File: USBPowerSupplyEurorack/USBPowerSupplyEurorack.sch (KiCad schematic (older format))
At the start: 21 parts, among them J1 1734366-1, J2 95278-501A10LF, Q1 Q_PMOS_GSD

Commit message: added LEDs, all components are placed now
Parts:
- D2, D5: footprint (none) -> digikey-footprints:LED_0603
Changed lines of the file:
@@
 F 0 "D2" V 3121 5260 50  0000 R CNN
 F 1 "Blue" V 3030 5260 50  0000 R CNN
-F 2 "" V 3075 5330 50  0001 C CNN
+F 2 "digikey-footprints:LED_0603" V 3075 5330 50  0001 C CNN
 F 3 "~" V 3075 5330 50  0001 C CNN
 	1    3075 5330
@@
 F 0 "D5" V 3121 5850 50  0000 R CNN
 F 1 "Blue" V 3030 5850 50  0000 R CNN
-F 2 "" V 3075 5920 50  0001 C CNN
+F 2 "digikey-footprints:LED_0603" V 3075 5920 50  0001 C CNN
 F 3 "~" V 3075 5920 50  0001 C CNN
 	1    3075 5920

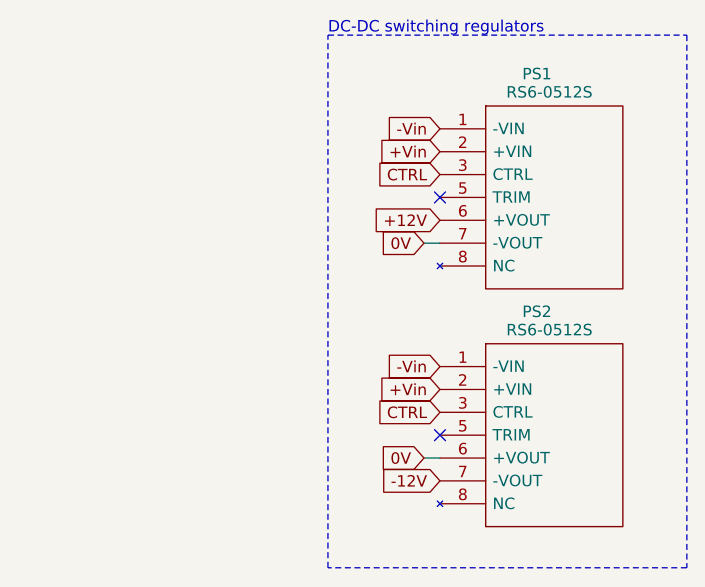
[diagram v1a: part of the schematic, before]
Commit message: new naive routing
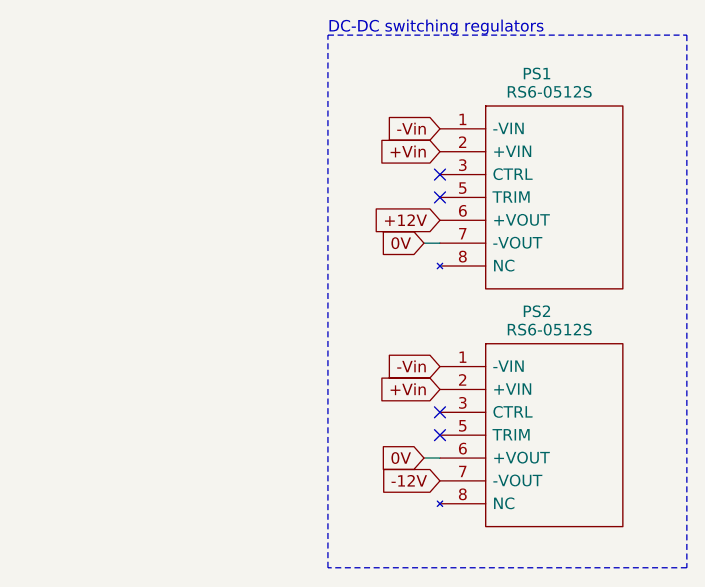
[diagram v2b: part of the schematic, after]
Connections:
- net CTRL: no longer names the net of PS1.3 (CTRL)
- net CTRL: no longer PS2.3 (CTRL)
- no-connect marks 4 -> 6
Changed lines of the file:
@@
 Wire Wire Line
 	8800 3190 8870 3190
-$Comp
-L RS6-0512S:RS6-0512S PS2
-U 1 1 5FE68DDD
-P 8870 3730
-F 0 "PS2" H 9230 3970 50  0000 L CNN
-F 1 "RS6-0512S" H 9160 3890 50  0000 L CNN
-F 2 "RS6-0512S:RS60512S" H 9720 3830 50  0001 L CNN
-F 3 "https://componentsearchengine.com/Datasheets/1/RS6-0512S.pdf" H 9720 3730 50  0001 L CNN
-F 4 "Isolated DC/DC Converters 6W 4.5-9Vin 12Vout 500mA SIP8" H 9720 3630 50  0001 L CNN "Description"
-F 5 "11.6" H 9720 3530 50  0001 L CNN "Height"
-F 6 "RECOM Power" H 9720 3430 50  0001 L CNN "Manufacturer_Name"
-F 7 "RS6-0512S" H 9720 3330 50  0001 L CNN "Manufacturer_Part_Number"
-F 8 "919-RS6-0512S" H 9720 3230 50  0001 L CNN "Mouser Part Number"
-F 9 "https://www.mouser.co.uk/ProductDetail/RECOM-Power/RS6-0512S?qs=FLBwGrBR9%252B1rp7zTwCRMhw%3D%3D" H 9720 3130 50  0001 L CNN "Mouser Price/Stock"
-F 10 "" H 9720 3030 50  0001 L CNN "Arrow Part Number"
-F 11 "" H 9720 2930 50  0001 L CNN "Arrow Price/Stock"
-	1    8870 3730
-	1    0    0    -1
-$EndComp
 Text GLabel 8870 3730 0    50   Input ~ 0
 -Vin
@@
 	1    0    0    -1
 $EndComp
-Text GLabel 8870 2890 0    50   Input ~ 0
-CTRL
 $Comp
 L RS6-0512S:RS6-0512S PS1
@@
 	1    0    0    -1
 $EndComp
-Text GLabel 8870 3930 0    50   Input ~ 0
-CTRL
 $Comp
 L ACP3225-102-2P-T000:ACP3225-102-2P-T000 FL1
@@
 Wire Wire Line
 	2250 2235 2250 2765
+$Comp
+L RS6-0512S:RS6-0512S PS2
+U 1 1 5FE68DDD
+P 8870 3730
+F 0 "PS2" H 9230 3970 50  0000 L CNN
+F 1 "RS6-0512S" H 9160 3890 50  0000 L CNN
+F 2 "RS6-0512S:RS60512S" H 9720 3830 50  0001 L CNN
+F 3 "https://componentsearchengine.com/Datasheets/1/RS6-0512S.pdf" H 9720 3730 50  0001 L CNN
+F 4 "Isolated DC/DC Converters 6W 4.5-9Vin 12Vout 500mA SIP8" H 9720 3630 50  0001 L CNN "Description"
+F 5 "11.6" H 9720 3530 50  0001 L CNN "Height"
+F 6 "RECOM Power" H 9720 3430 50  0001 L CNN "Manufacturer_Name"
+F 7 "RS6-0512S" H 9720 3330 50  0001 L CNN "Manufacturer_Part_Number"
+F 8 "919-RS6-0512S" H 9720 3230 50  0001 L CNN "Mouser Part Number"
+F 9 "https://www.mouser.co.uk/ProductDetail/RECOM-Power/RS6-0512S?qs=FLBwGrBR9%252B1rp7zTwCRMhw%3D%3D" H 9720 3130 50  0001 L CNN "Mouser Price/Stock"
+F 10 "" H 9720 3030 50  0001 L CNN "Arrow Part Number"
+F 11 "" H 9720 2930 50  0001 L CNN "Arrow Price/Stock"
+	1    8870 3730
+	1    0    0    -1
+$EndComp
+NoConn ~ 8870 2890
+NoConn ~ 8870 3930
 $EndSCHEMATC

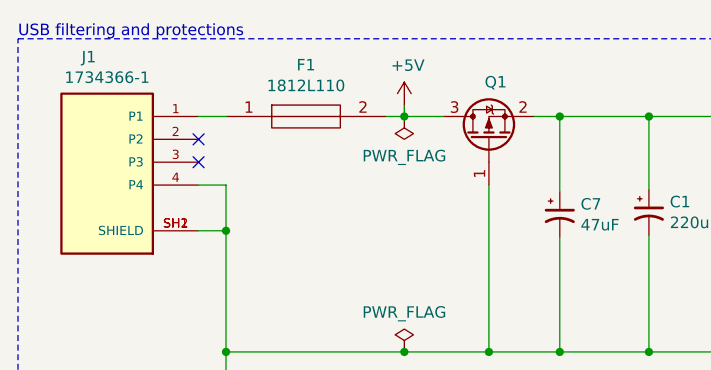
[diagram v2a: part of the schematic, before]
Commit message: going to 4hp for better routing
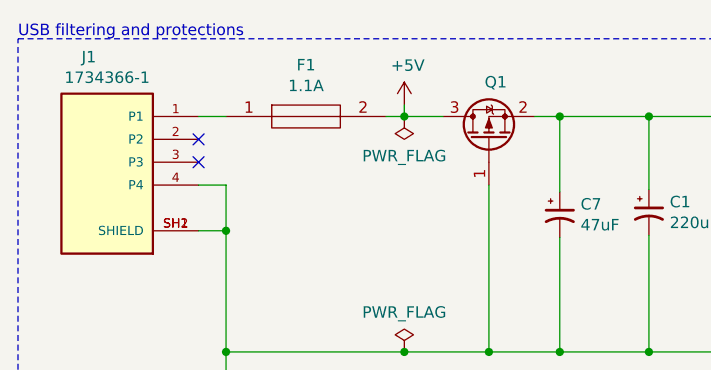
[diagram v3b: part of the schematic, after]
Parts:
- F1: value 1812L110 -> 1.1A
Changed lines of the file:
@@
 P 2250 1735
 F 0 "F1" H 2600 1960 50  0000 C CNN
-F 1 "1812L110" H 2600 1869 50  0000 C CNN
+F 1 "1.1A" H 2600 1869 50  0000 C CNN
 F 2 "Fuse:Fuse_1812_4532Metric" H 2800 1785 50  0001 L CNN
 F 3 "https://www.arrow.com/en/products/1812l11016dr/littelfuse" H 2800 1685 50  0001 L CNN

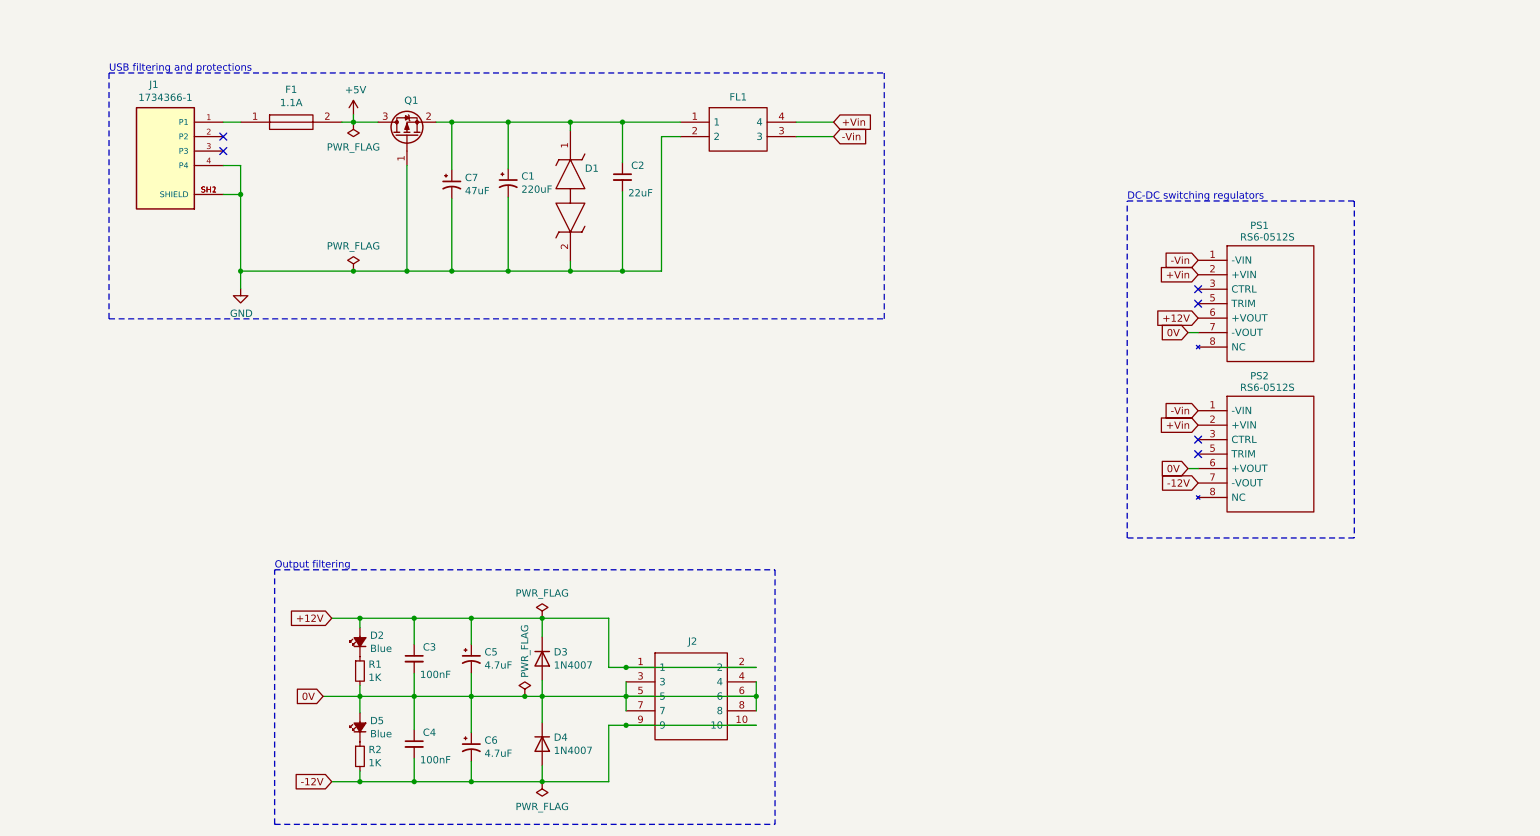
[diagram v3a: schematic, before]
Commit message: changed caps on schematics, added PI filter and bigger caps as we have now 4HP
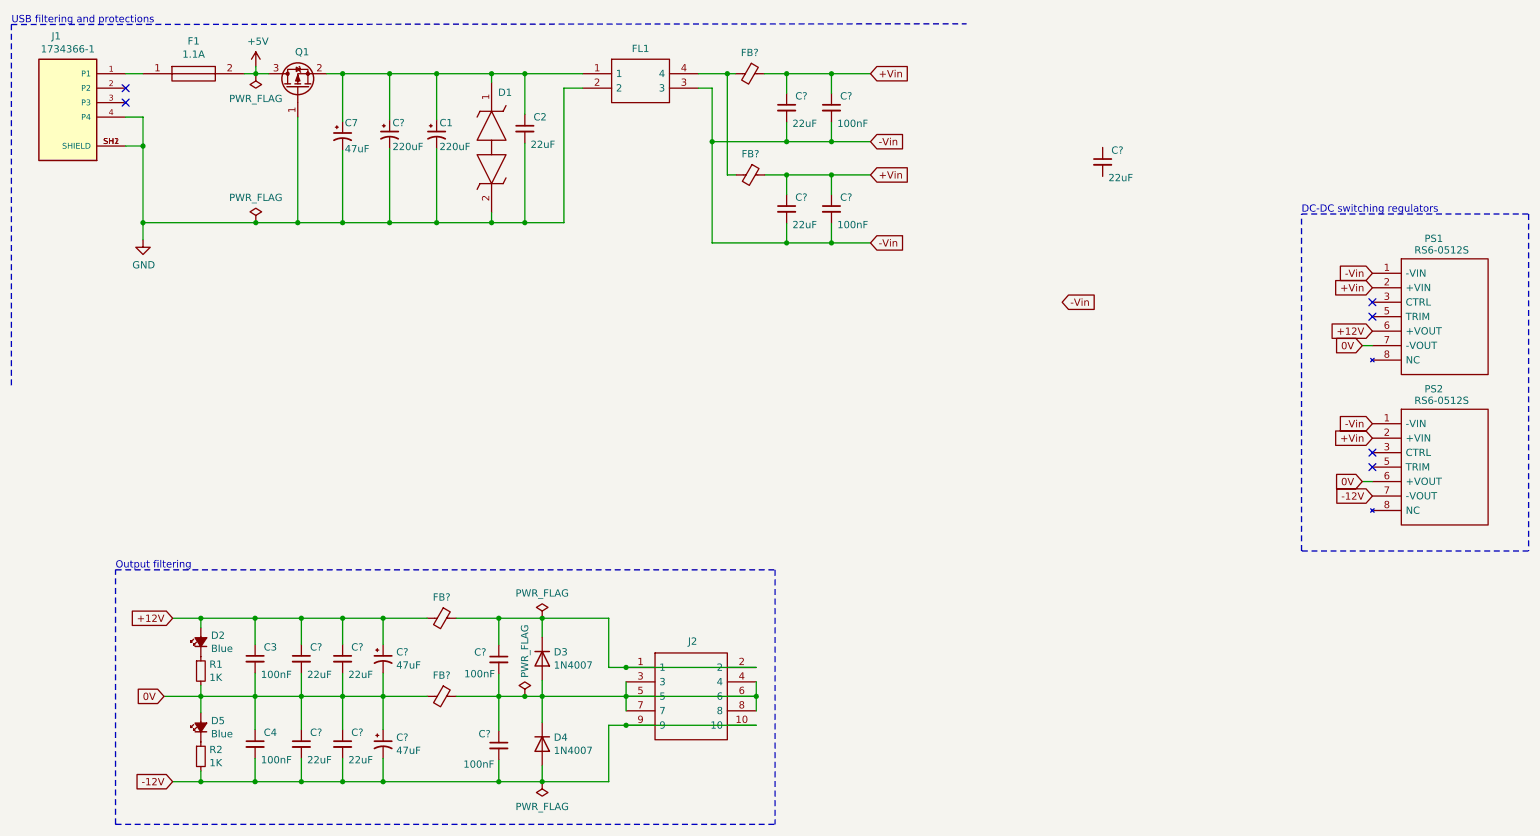
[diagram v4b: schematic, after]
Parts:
- removed C5, C6: 4.7uF, Capacitor_SMD:C_Elec_4x5.4, symbol Device:CP1_Small
- added C? (x7): 22uF, Capacitor_SMD:C_0805_2012Metric, symbol Device:C_Small
- added C? (x4): 100nF, Capacitor_SMD:C_0402_1005Metric, symbol Device:C_Small
- added C? (x2): 47uF, Capacitor_SMD:C_Elec_5x5.4, symbol Device:CP1_Small
- added C?: 220uF, Capacitor_SMD:C_Elec_6.3x7.7, symbol Device:CP1_Small
- added FB? (x4): C15957, symbol Device:Ferrite_Bead_Small
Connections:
- net +12V: now also C?.1, C?.1, C?.1, FB?.2; no longer D3.1 (K), J2.1, J2.2
- net +Vin: now also C?.1, C?.1, C?.1, C?.1, FB?.1, FB?.1; no longer FL1.4
- net -12V: now also C?.2, C?.2, C?.2, C?.2
- net -Vin: now also C?.2, C?.2, C?.2, C?.2
- net 0V: now also C?.1, C?.1, C?.1, C?.2, C?.2, C?.2, FB?.2; no longer D3.2 (A), D4.1 (K), J2.3, J2.4, J2.5, J2.6, J2.7, J2.8
- net GND: now also C?.2
- net at C1.1, C2.1, C7.1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: now also C?.1
- new net: C?.1, D3.1 (K), FB?.1, J2.1, J2.2
- new net: C?.1, C?.2, D3.2 (A), D4.1 (K), FB?.1, J2.3, J2.4, J2.5, J2.6, J2.7, J2.8
- new net: FB?.2, FB?.2, FL1.4
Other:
- moved on the sheet: C1, C2, C3, C4, C7, D1, D2, D5, F1, FL1, J1, PS1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

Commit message: updated footprints
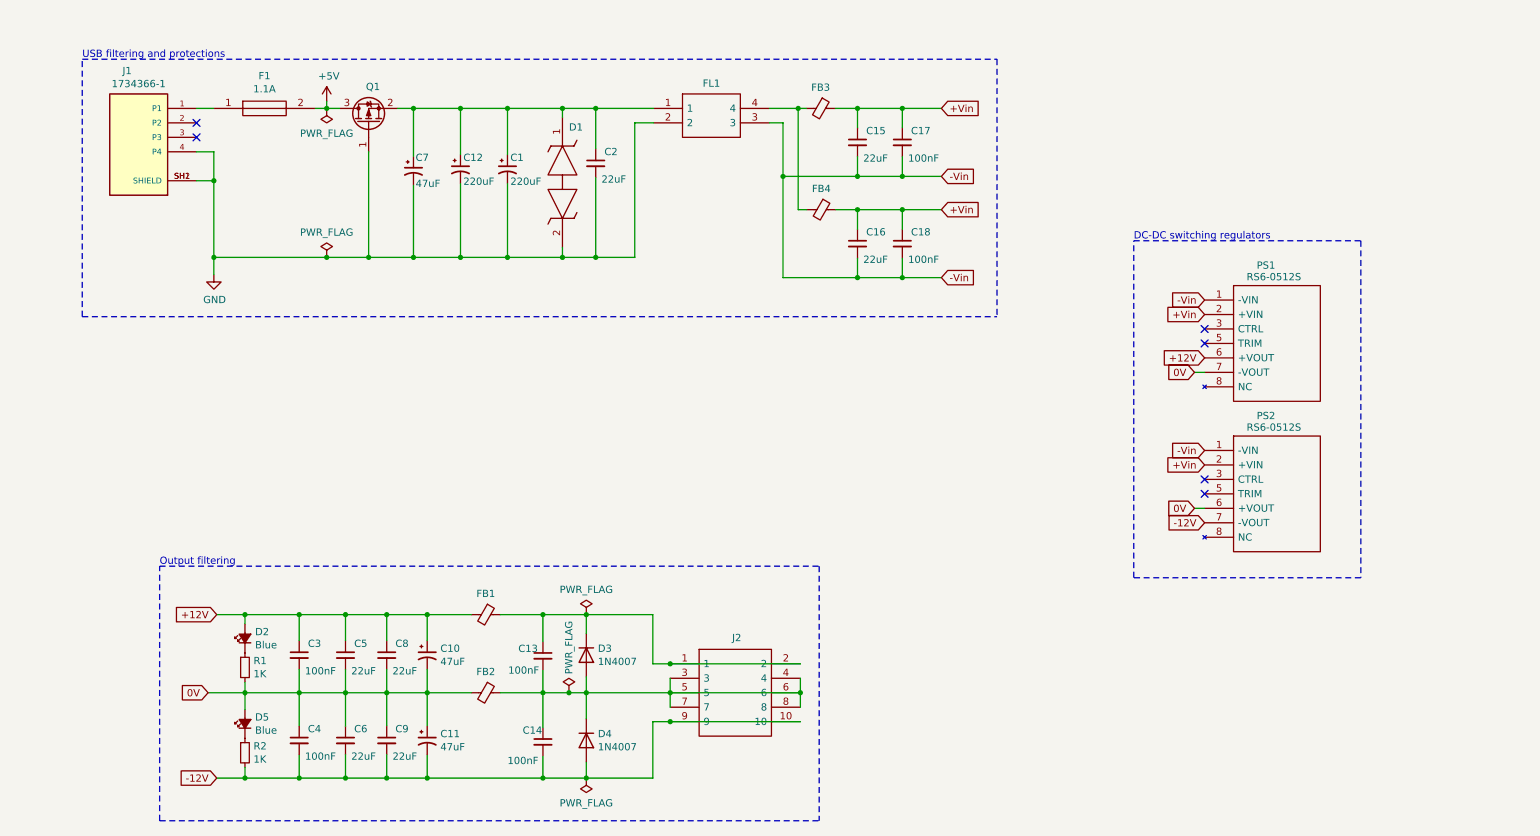
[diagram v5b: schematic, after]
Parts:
- removed C?: 22uF, Capacitor_SMD:C_0805_2012Metric, symbol Device:C_Small
- FB1, FB2, FB3, FB4: renamed from FB?; footprint (none) -> MPZ2012S101AT000:BEADC2012X105N
- gave numbers to parts that had none: 13
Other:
- moved on the sheet: C1, C10, C11, C12, C13, C14, C15, C16, C17, C18, C2, C3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

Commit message: new components placement
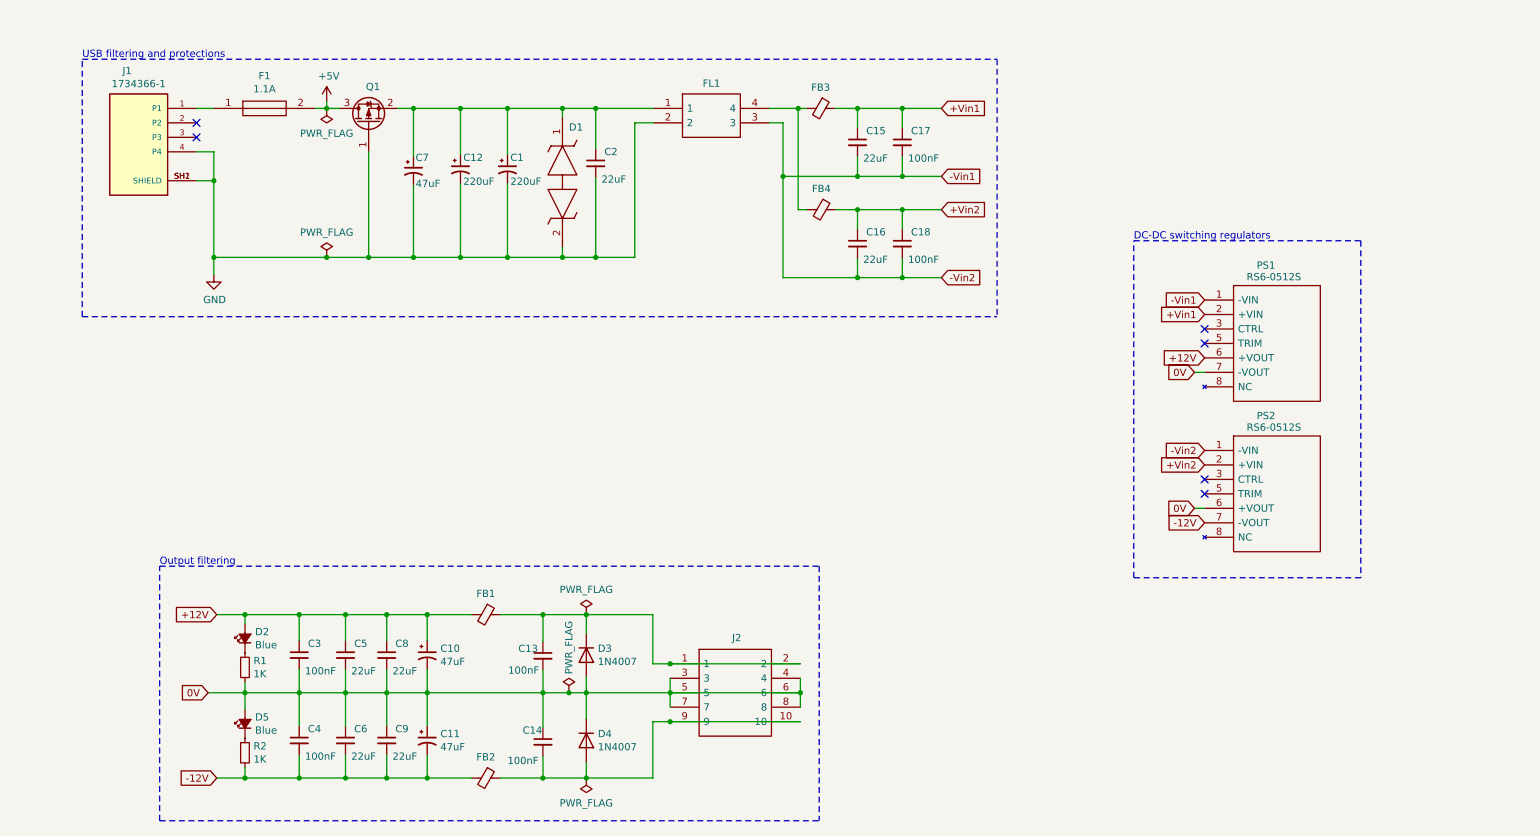
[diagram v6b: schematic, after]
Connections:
- net -12V: now also FB2.2; no longer C14.2, D4.2 (A), J2.10, J2.9
- net 0V: now also C13.2, C14.1, D3.2 (A), D4.1 (K), J2.3, J2.4, J2.5, J2.6, J2.7, J2.8; no longer FB2.2
- net +Vin renamed +Vin1
- net +Vin1: no longer C16.1, C18.1, FB4.1, PS2.2 (+VIN)
- net -Vin renamed -Vin1
- new net: C14.2, D4.2 (A), FB2.1, J2.10, J2.9
- new net +Vin2: C16.1, C18.1, FB4.1, PS2.2 (+VIN)
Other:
- moved on the sheet: FB2
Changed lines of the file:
@@
 DC-DC switching regulators
 Text GLabel 8915 2965 0    50   Input ~ 0
--Vin
+-Vin1
 Text GLabel 8915 3065 0    50   Input ~ 0
-+Vin
++Vin1
 Text GLabel 8845 3465 0    50   Input ~ 0
 0V
@@
 	8845 3465 8915 3465
 Text GLabel 8915 4005 0    50   Input ~ 0
--Vin
+-Vin2
 Text GLabel 8915 4105 0    50   Input ~ 0
-+Vin
++Vin2
 Text GLabel 8845 4405 0    50   Input ~ 0
 0V
@@
 	3770 2670 4095 2670
 Text GLabel 7095 1640 2    50   Input ~ 0
-+Vin
++Vin1
 Wire Wire Line
 	6825 1640 6515 1640
@@
 Connection ~ 6825 2110
 Text GLabel 7095 2110 2    50   Input ~ 0
--Vin
+-Vin1
 Wire Wire Line
 	6825 2110 7095 2110
 Text GLabel 7095 2340 2    50   Input ~ 0
-+Vin
++Vin2
 $Comp
 L Device:C_Small C16
@@
 	6825 2810 7095 2810
 Text GLabel 7095 2810 2    50   Input ~ 0
--Vin
+-Vin2
 Wire Wire Line
 	5905 1740 6000 1740
@@
 	3540 6270 3260 6270
 Connection ~ 3540 5680
-Connection ~ 3540 6270
 $Comp
 L Device:CP1_Small C10
@@
 	4340 6120 4340 6270
 Wire Wire Line
-	3540 6270 4340 6270
-Wire Wire Line
 	4340 6270 4640 6270
-Connection ~ 4340 6270
 $Comp
 L Device:C_Small C13
@@
 L Device:Ferrite_Bead_Small FB2
 U 1 1 60111921
-P 3945 5680
-F 0 "FB2" V 3800 5680 50  0000 C CNN
-F 1 "C15957" V 3799 5680 50  0001 C CNN
-F 2 "MPZ2012S101AT000:BEADC2012X105N" V 3875 5680 50  0001 C CNN
-F 3 "~" H 3945 5680 50  0001 C CNN
-F 4 "C15957" V 3945 5680 50  0001 C CNN "LSCS"
-	1    3945 5680
+P 3945 6270
+F 0 "FB2" V 3800 6270 50  0000 C CNN
+F 1 "C15957" V 3799 6270 50  0001 C CNN
+F 2 "MPZ2012S101AT000:BEADC2012X105N" V 3875 6270 50  0001 C CNN
+F 3 "~" H 3945 6270 50  0001 C CNN
+F 4 "C15957" V 3945 6270 50  0001 C CNN "LSCS"
+	1    3945 6270
 	0    1    1    0
 $EndComp
-Wire Wire Line
-	3845 5680 3540 5680
-Wire Wire Line
-	4045 5680 4340 5680
 Wire Notes Line
 	7480 1300 7480 3080
@@
 Wire Notes Line
 	1155 3080 7480 3080
+Wire Wire Line
+	3845 6270 3540 6270
+Connection ~ 3540 6270
+Wire Wire Line
+	4045 6270 4340 6270
+Connection ~ 4340 6270
+Wire Wire Line
+	3540 5680 4340 5680
 $EndSCHEMATC
